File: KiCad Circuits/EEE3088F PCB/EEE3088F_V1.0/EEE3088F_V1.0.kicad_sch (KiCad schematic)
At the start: 48 parts, among them J1 Conn_01x02_Pin, J2 Conn_02x16_Odd_Even, U1 MT3608, U2 INA219AxD, U3 DRV8833PWP, U4 AP2112K-3.3, U5 DRV8833PWP, U6 BQ24074RGT, U7 AP2171W, U8 AP2171W

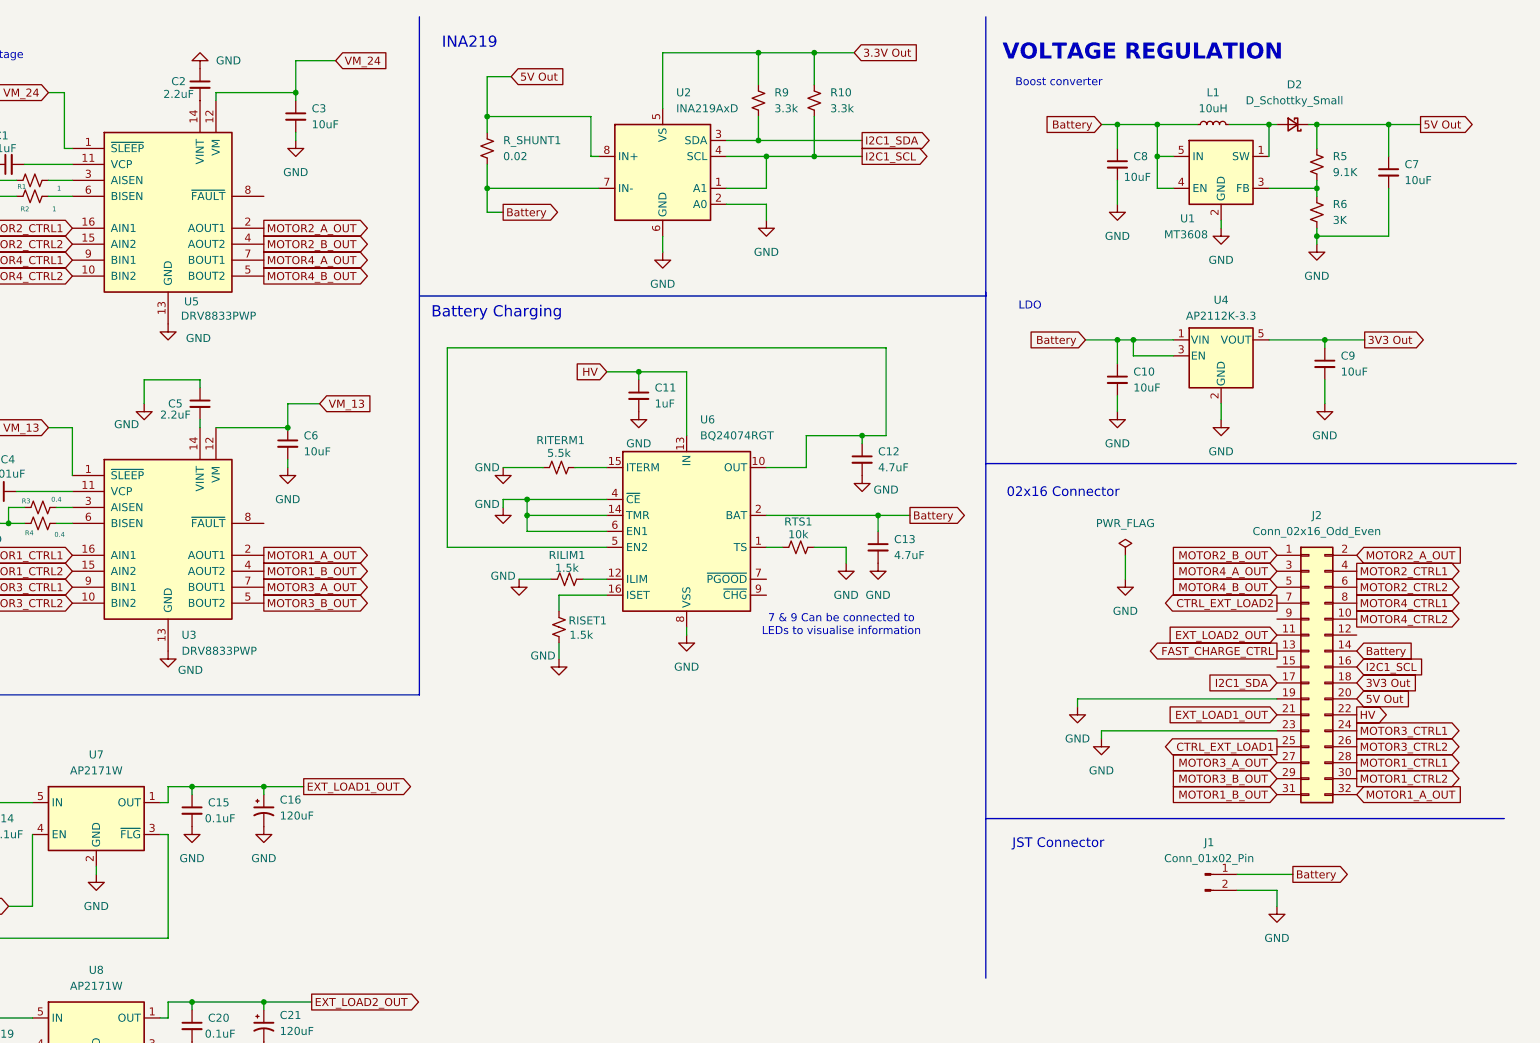
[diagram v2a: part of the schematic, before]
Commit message: Analogue Switch added
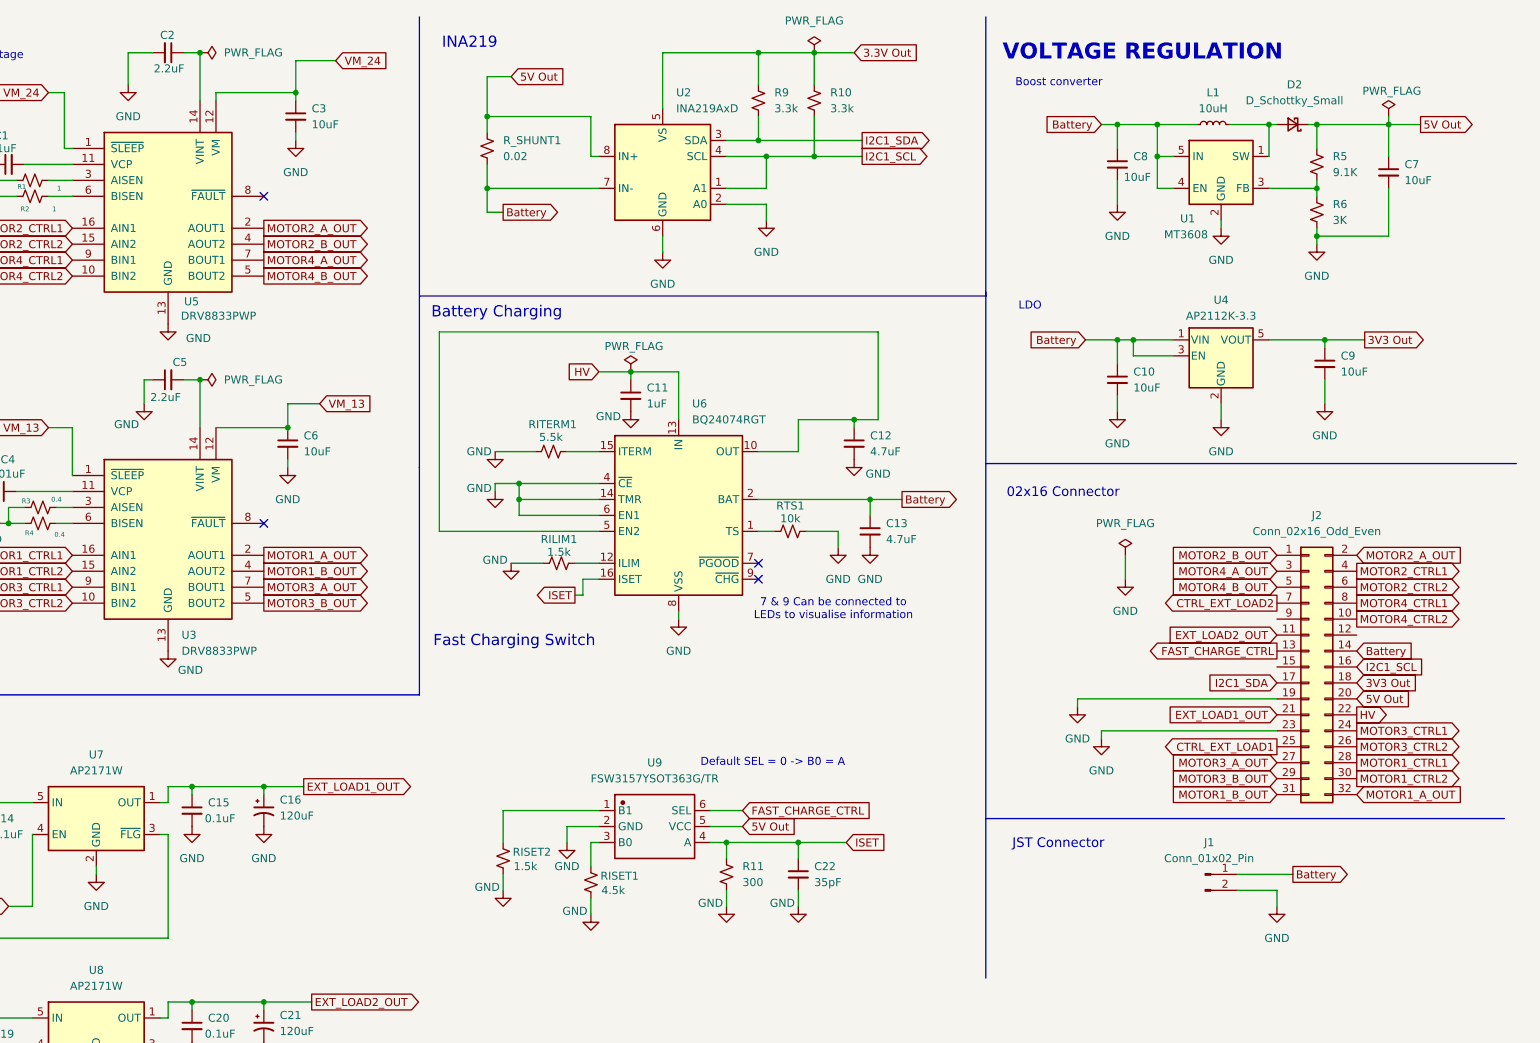
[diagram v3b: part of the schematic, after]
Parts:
- added C22: 35pF, symbol Device:C_Small
- added R11: 300, symbol Device:R_Small_US
- added RISET2: 1.5k, symbol Device:R_Small_US
- added U9: FSW3157YSOT363G/TR, symbol New_Library:FSW3157YSOT363G/TR
- RISET1: value 1.5k -> 4.5k
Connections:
- net 5V Out: now also U9.5 (VCC)
- net FAST_CHARGE_CTRL: now also U9.6 (SEL)
- net GND: now also C2.2, C22.2, R11.2, RISET2.2, U9.2 (GND); no longer C2.1
- net at U5.14 (VINT): now also C2.1; no longer C2.2
- net at RISET1.1: now also U9.3 (B0); no longer U6.16 (ISET)
- new net: RISET2.1, U9.1 (B1)
- new net ISET: C22.1, R11.1, U6.16 (ISET), U9.4 (A)
- no-connect marks 0 -> 4
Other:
- note added: "Default SEL = 0 -> B0 = A"
- note added: "Fast Charging Switch"
- moved on the sheet: C11, C12, C13, C2, C5, RILIM1, RISET1, RITERM1, RTS1, U6

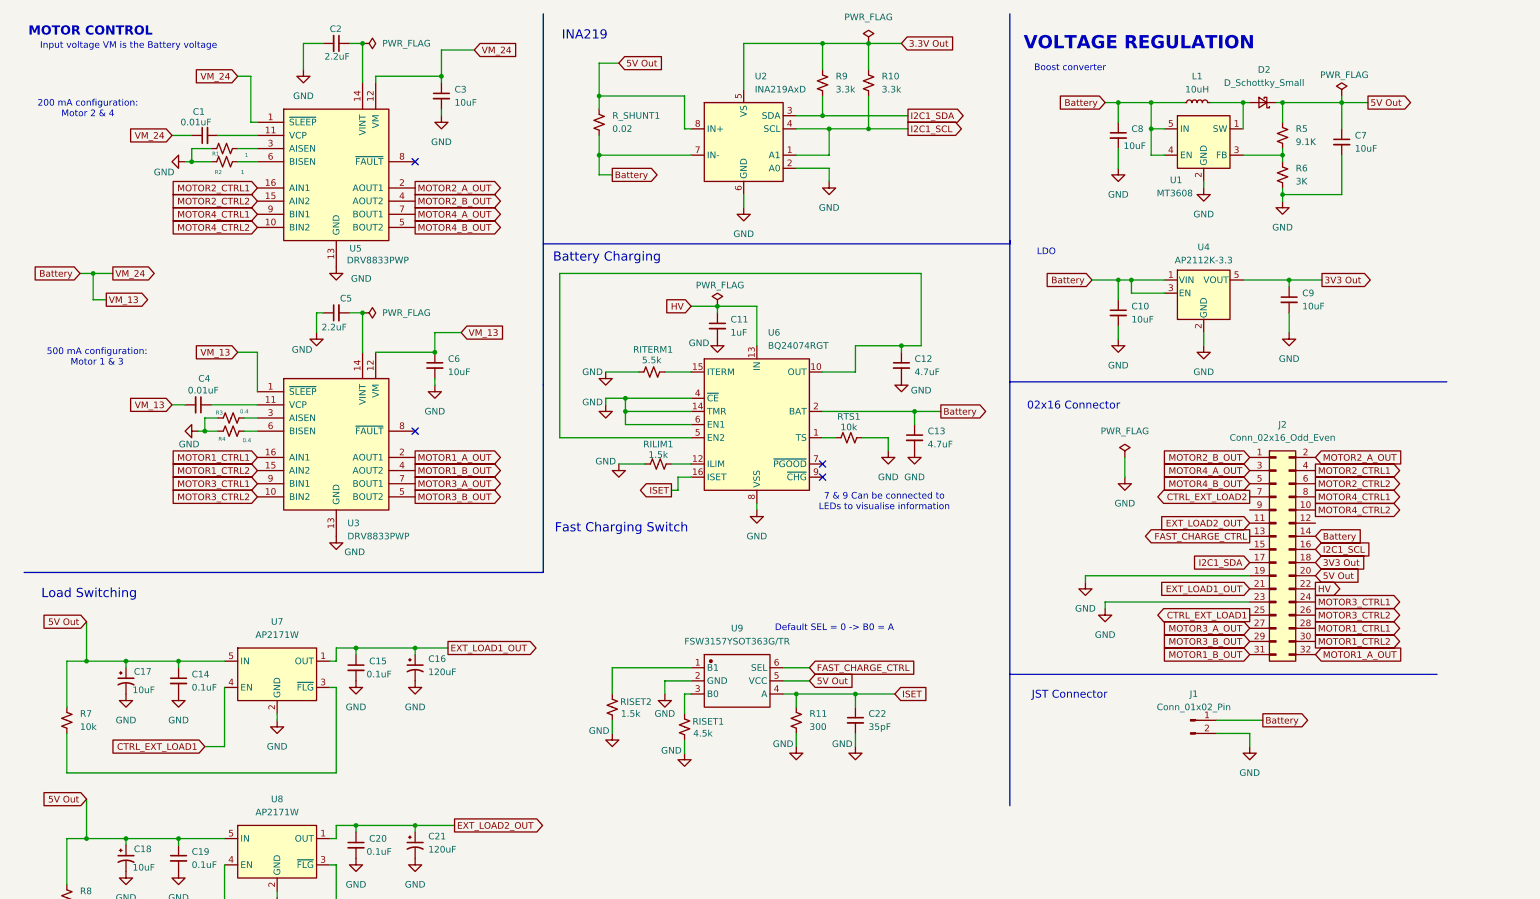
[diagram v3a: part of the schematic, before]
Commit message: Added Mechanical Switch
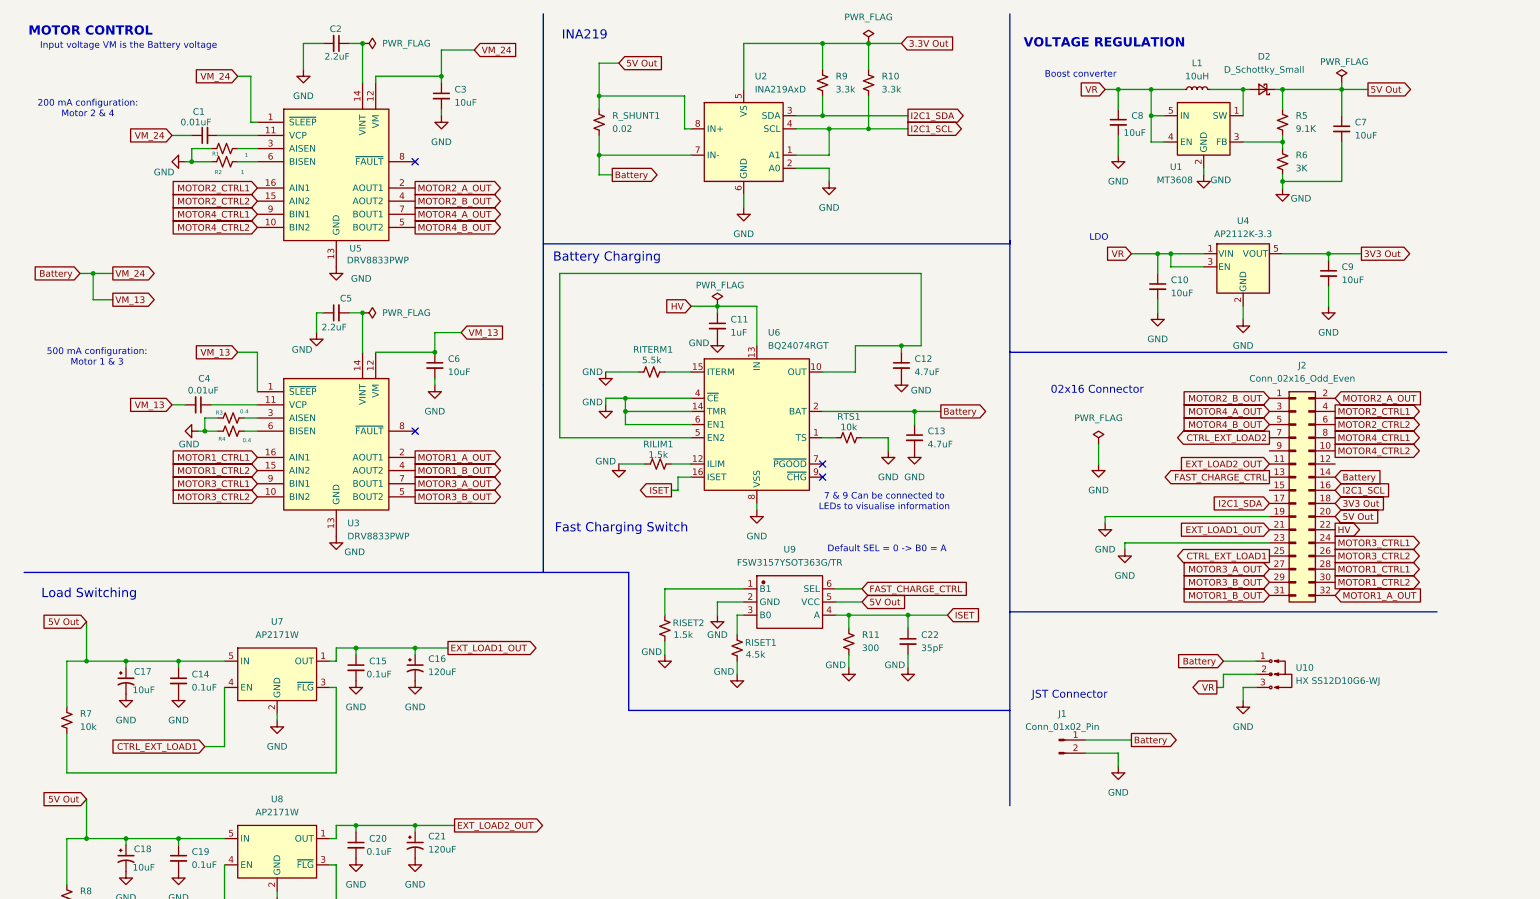
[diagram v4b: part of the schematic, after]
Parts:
- added U10: HX SS12D10G6-WJ, symbol New_Library:HX SS12D10G6-WJ
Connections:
- net Battery: now also U10.1; no longer C10.1, C8.1, L1.1, U1.4 (EN), U1.5 (IN), U4.1 (VIN), U4.3 (EN)
- net GND: now also U10.3
- new net VR: C10.1, C8.1, L1.1, U1.4 (EN), U1.5 (IN), U10.2, U4.1 (VIN), U4.3 (EN)
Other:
- moved on the sheet: C10, C22, C7, C8, C9, D2, J1, J2, L1, R11, R5, R6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

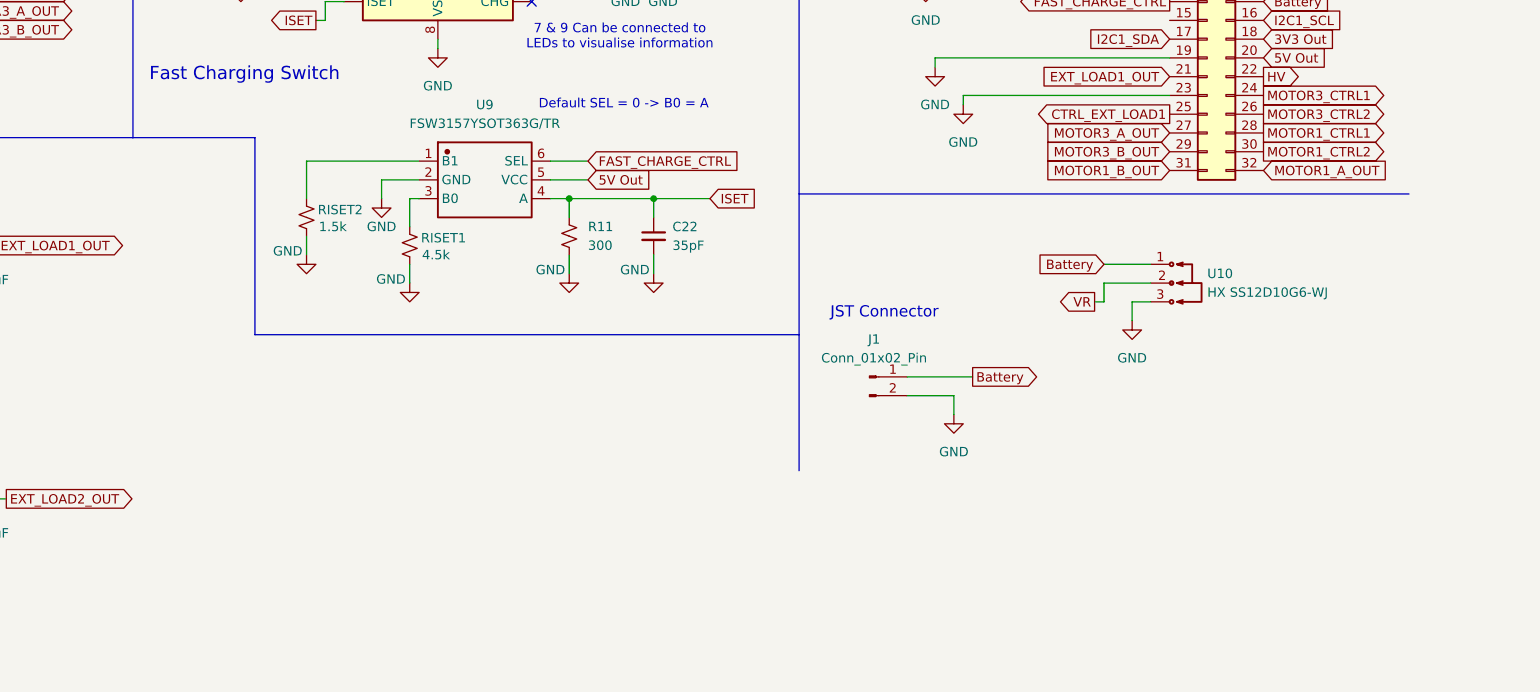
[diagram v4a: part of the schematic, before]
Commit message: added symbols
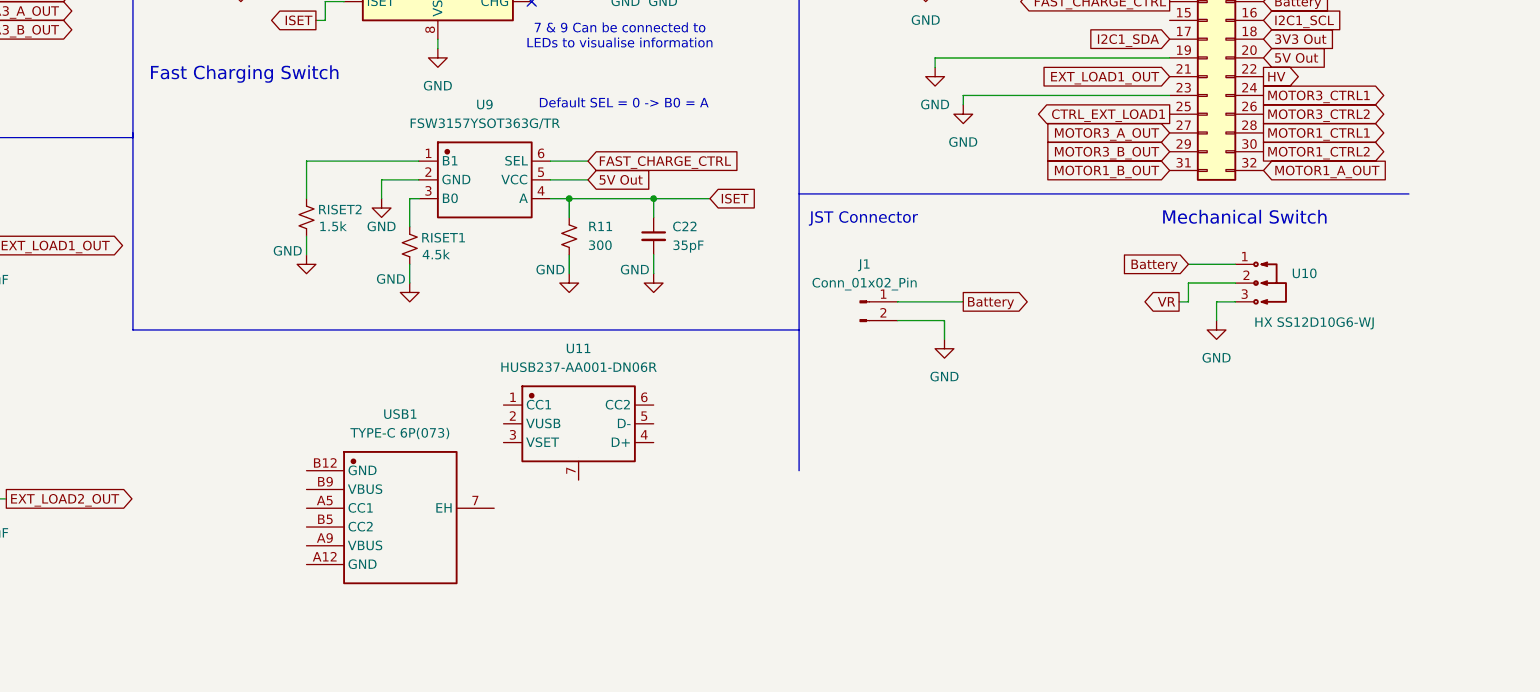
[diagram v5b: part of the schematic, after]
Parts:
- added U11: HUSB237-AA001-DN06R, symbol New_Library:HUSB237-AA001-DN06R
- added USB1: TYPE-C 6P(073), symbol New_Library:TYPE-C 6P(073)
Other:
- note added: "Mechanical Switch"
- moved on the sheet: J1, U10

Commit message: Increased page size and added footprint to imported components
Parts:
- U10: footprint (none) -> Footprints:SW-TH_3P-P4.80_HX-SS12D10G6-WJ
- U11: footprint (none) -> Footprints:TDFN-6_L2.0-W2.0-P0.65-TL-EP
- U9: footprint (none) -> Footprints:SOT-363_L2.1-W1.3-P0.65-LS2.1-BL
- USB1: footprint (none) -> Footprints:TYPE-C-SMD_TYPE-C-6P_5
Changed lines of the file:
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@@
 	(generator "eeschema")
 	(generator_version "9.0")
-	(paper "A4")
+	(paper "A3")
 	(title_block
 		(title "EEE3088F PCB Circuit")
@@
 			)
 		)
-		(property "Footprint" ""
+		(property "Footprint" "Footprints:SOT-363_L2.1-W1.3-P0.65-LS2.1-BL"
 			(at 160.02 125.73 0)
 			(effects
@@
 			)
 		)
-		(property "Footprint" ""
+		(property "Footprint" "Footprints:TDFN-6_L2.0-W2.0-P0.65-TL-EP"
 			(at 172.72 158.75 0)
 			(effects
@@
 			)
 		)
-		(property "Footprint" ""
+		(property "Footprint" "Footprints:TYPE-C-SMD_TYPE-C-6P_5"
 			(at 148.59 170.18 0)
 			(effects
@@
 			)
 		)
-		(property "Footprint" ""
+		(property "Footprint" "Footprints:SW-TH_3P-P4.80_HX-SS12D10G6-WJ"
 			(at 264.16 139.7 0)
 			(effects
